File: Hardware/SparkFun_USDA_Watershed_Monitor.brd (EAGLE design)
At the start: 63.5 x 50.8 mm, 113 parts, among them J3 QWIIC_RIGHT_ANGLE, J4 U.FL, Q1 20V/4.2A/52mΩ/1.4W, Q2 20V/0.2A/8MHz/1.2Ω/1Vth, Q3 20V/0.2A/8MHz/1.2Ω/1Vth, Q4 20V/0.2A/8MHz/1.2Ω/1Vth, Q5 20V/0.2A/8MHz/1.2Ω/1Vth, U1 ESP-WROOM-3232D, U10 MMC5983MA_QFN16, U11 RFM9XRFM95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

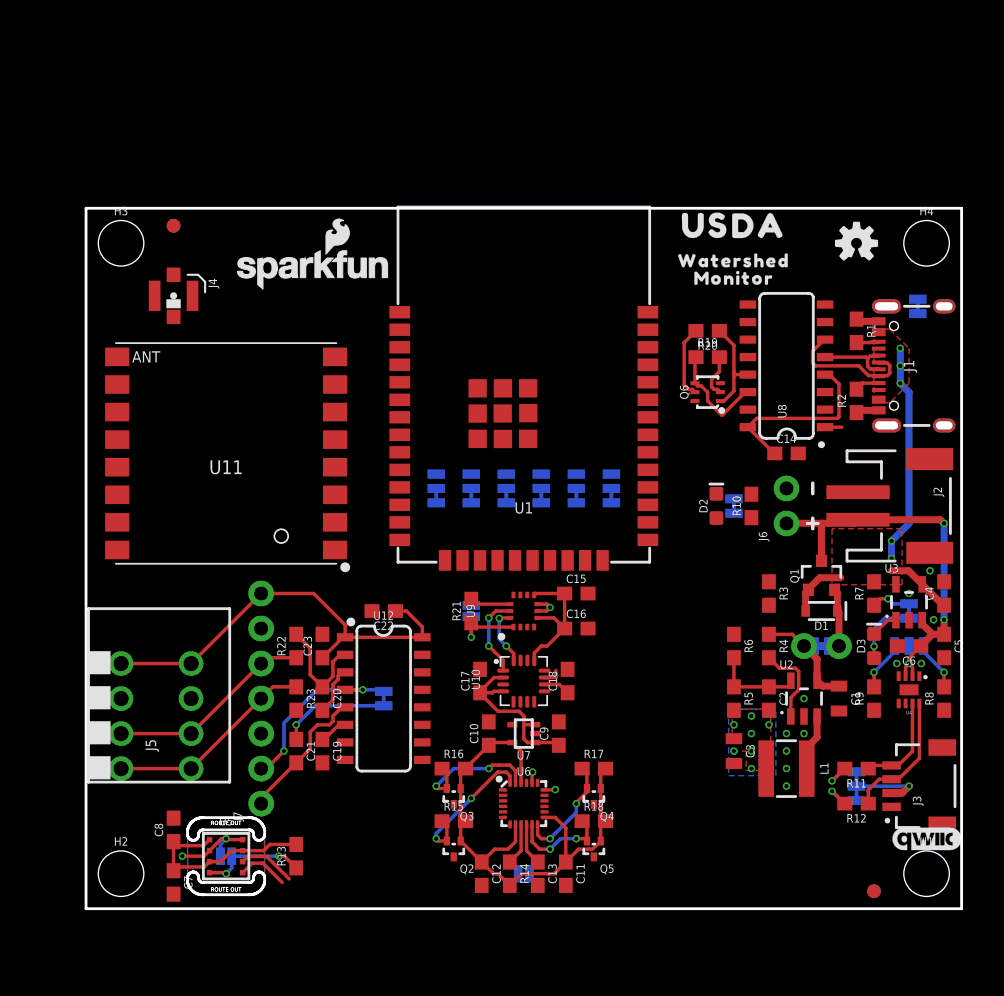
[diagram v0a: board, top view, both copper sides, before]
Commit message: Finish 90% of initial design
Rename Eagle files to match project name
Clean up schematic arrangement
Finish 90% of routing (ESP32 connections will be determined later)
Add Buzzard labels
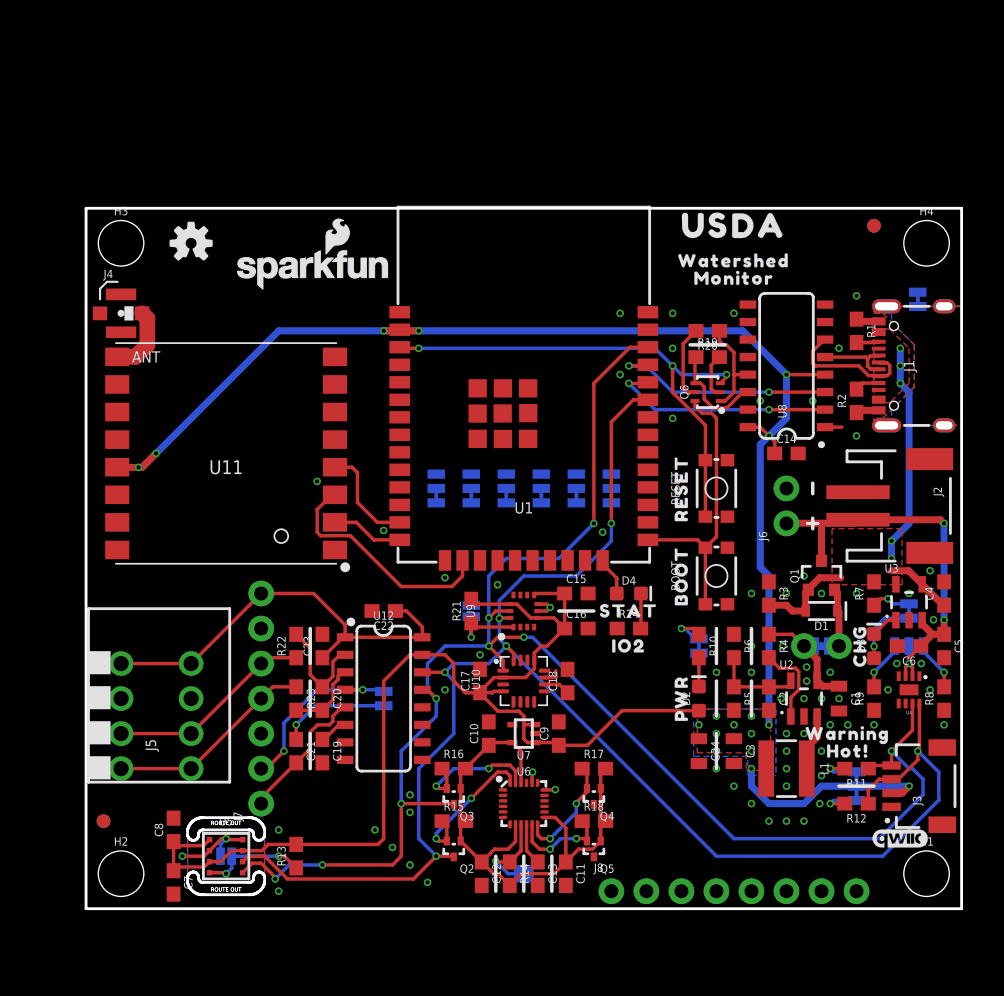
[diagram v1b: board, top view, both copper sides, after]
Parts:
- added BOOT, RESET: MOMENTARY-SWITCH-SPST-SMD-4.6X2.8MM, SparkFun-Switches:TACTILE_SWITCH_SMD_4.6X2.8MM
- added C24: 22uF, SparkFun-Capacitors:0805
- added D4: BLUE, SparkFun-LED:LED-0603
- added J8: (no value), SparkFun-Connectors:1X08_NO_SILK
- added R24: 2.2k, SparkFun-Resistors:0603
- added U$12: (no value), output:#100MA#0
- added U$13: (no value), output:#500MA#0
- added U$14: (no value), output:#CHG#0
- added U$15: (no value), output:#I2C#0
- added U$16: (no value), output:CHG0
- added U$17: (no value), output:#CAP#0
- added U$18: (no value), output:#BME_ADR#0
- added U$19: (no value), output:#ICM_ADR#0
- added U$20: (no value), output:#ISM_ADR#0
- added U$21: (no value), output:#BATTERY#0
- added U$22: (no value), output:#SHLD#0
- added U$23, U$24: (no value), output:WARNING0
- added U$25, U$26: (no value), output:HOT##0
- added U$27: (no value), output:RESET0
- added U$28: (no value), output:BOOT0
- added U$29: (no value), output:PWR0
- added U$30: (no value), output:STAT0
- added U$31: (no value), output:IO20
- added U$9: (no value), output:#MEAS#0
- LOGO3: value QWIIC_LOGO_5MM -> QWIIC_LOGO_4MM; device SparkFun-Aesthetics:QWIIC_5MM -> SparkFun-Aesthetics:QWIIC_4MM
- moved FD1 56.1 mm to (1.27, 6.35)
- moved FD2 56.1 mm to (1.27, 6.35)
- moved FD3 50.8 mm to (57.1, 49.5)
- moved FD4 50.8 mm to (57.1, 49.5)
- moved LOGO2 48.3 mm to (7.62, 48.3)
- moved D2 14.0 mm to (44.5, 15.2)
- moved R10 10.9 mm to (44.5, 19.1), turned to 270 degrees
- moved PWR 10.5 mm to (44.5, 19.1)
- moved J4 4.02 mm to (2.54, 43.2), turned to 0 degrees
- moved LOGO3 1.91 mm to (59.1, 5.08)
- moved SHLD 0.51 mm to (60.3, 44.2)
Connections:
- net N$1 renamed SHLD
- new net N$1: D4.C, R24.2
- net 3.3V: now also C24.1
- net ESP_EN: now also RESET.3, RESET.4
- net ESP_IO0: now also BOOT.3, BOOT.4
- net ESP_IO2: now also D4.A
- net GND: now also BOOT.1, BOOT.2, C24.2, R24.1, RESET.1, RESET.2
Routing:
- net 3.3V: track 59.9 -> 191.6 mm, vias 8 -> 17
- net SCL: track 16.9 -> 122.1 mm, vias 2 -> 9
- net SDA: track 18.1 -> 119.5 mm, vias 2 -> 6
- net ESP_EN: track 0.00 -> 37.3 mm, vias 0 -> 3
- net ESP_IO0: track 0.00 -> 20.5 mm
- net PICO: track 0.00 -> 17.0 mm
- net ESP_TX: track 0.00 -> 16.4 mm, vias 0 -> 2
- net ESP_RX: track 0.00 -> 16.4 mm, vias 0 -> 2
- net SCK: track 0.00 -> 7.61 mm
- net POCI: track 0.00 -> 5.22 mm
- net N$25: track 0.00 -> 4.99 mm
- net N$17: track 3.07 -> 6.09 mm, vias 0 -> 1
- net N$26: track 0.00 -> 3.02 mm, vias 0 -> 1
- net V_USB: track 25.2 -> 28.1 mm
- net ESP_IO2: track 0.00 -> 2.83 mm
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- added copper zone on layer 1, net SHLD
- added copper zone on layer 16, net SHLD

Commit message: Finish initial design
Increase board height from 2 to 2.5 inches
Move LoRa module up, and antenna to top side of board
Replace load cell spring terminal and GPIO header with RJ45 jacks
Add second Qwiic connector to left side of board
Remove fuel gauge
Remove CHG_I jumper, and set charge current to 500mA only
Reroute I2C lines to make room for GPIO going to bottom of the board
Connect and route GPIO lines to bottom RJ45 connectors
Adjust/add buzzard labels
Add region on back silk for board notes
Season with GND vias
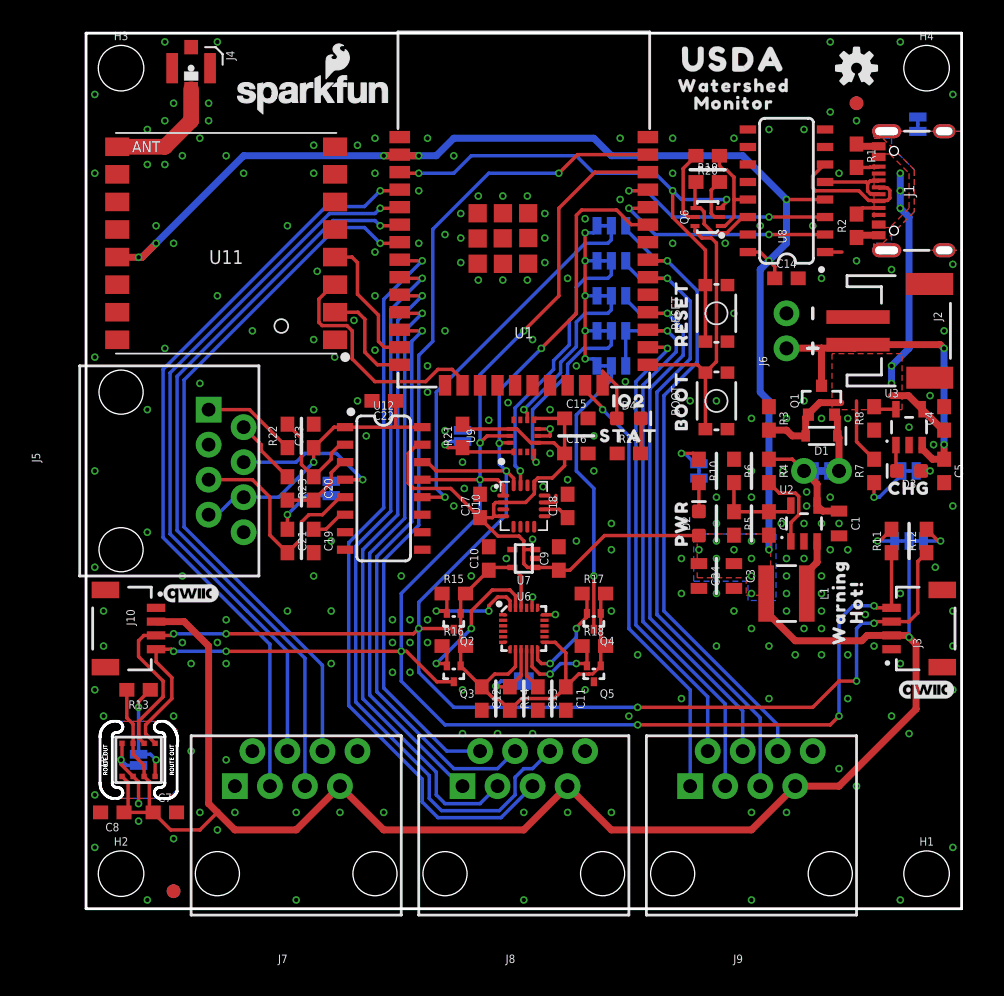
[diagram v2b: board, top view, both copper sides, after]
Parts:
- removed C6: 0.1uF, SparkFun-Capacitors:0603
- removed CHG_I, MAX_INT: JUMPER-SMT_3_1-NC_TRACE_SILK, SparkFun-Jumpers:SMT-JUMPER_3_1-NC_TRACE_SILK
- removed R9: 10k, SparkFun-Resistors:0603
- removed U4: MAX17048, SparkFun-IC-Power:DFN-8
- added J10: QWIIC_RIGHT_ANGLE, SparkFun-Connectors:JST04_1MM_RA
- added J9: RJ45, SparkFun-Connectors:RJ45-8
- added LOGO4: QWIIC_LOGO_4MM, SparkFun-Aesthetics:QWIIC_4MM
- added U$32: (no value), output:ORW0
- added U$33: (no value), output:OR0
- added U$34: (no value), output:GRW0
- added U$35: (no value), output:GR0
- added U$36: (no value), output:BLW0
- added U$37: (no value), output:BL0
- added U$38: (no value), output:BRW0
- added U$39: (no value), output:BR0
- added U$40: (no value), output:A#1
- added U$41: (no value), output:B#0
- added U$42: (no value), output:B#1
- added U$43: (no value), output:E#0
- added U$44: (no value), output:E#1
- added U$45: (no value), output:#RJ45_COLORS#0
- added U$46: (no value), output:#PWR#0
- added U$47, U$48: (no value), output:NC0
- added U$49: (no value), output:IO270
- added U$50: (no value), output:IO260
- added U$51: (no value), output:IO230
- added U$52: (no value), output:IO250
- added U$53: (no value), output:IO320
- added U$54: (no value), output:IO330
- added U$55: (no value), output:IO150
- added U$56: (no value), output:IO40
- added U$57: (no value), output:IO160
- added U$58: (no value), output:IO170
- added U$59: (no value), output:IO180
- added U$60: (no value), output:IO190
- added U$61: (no value), output:I340
- added U$62: (no value), output:I350
- added U$63: (no value), output:I360
- added U$64: (no value), output:I390
- added U$65: (no value), output:#IO19#0
- added U$66: (no value), output:#IO18#0
- added U$67: (no value), output:#IO17#0
- added U$68, U$69: (no value), output:#IO16#0
- added U$70: (no value), output:#NAU_INT#0
- added U$71: (no value), output:#MMC_INT#0
- added U$72: (no value), output:#ISM_INT2#0
- added U$73: (no value), output:#ISM_INT1#0
- added U$74: (no value), output:#ICM_INT#0
- added U$75: (no value), output:#IO#0
- added U$76: (no value), output:##INT##0
- added U$77: (no value), output:#NOTES#0
- J5: value (none) -> RJ45; device SparkFun-Connectors:1X04_SPRING_TERMINAL -> SparkFun-Connectors:RJ45-8
- J7: value (none) -> RJ45; device SparkFun-Connectors:1X07_NO_SILK -> SparkFun-Connectors:RJ45-8
- J8: value (none) -> RJ45; device SparkFun-Connectors:1X08_NO_SILK -> SparkFun-Connectors:RJ45-8
- U$10: device output:#B#_#0 -> output:3V30
- U$11: device output:#B#_#1 -> output:GND0
- U$12: device output:#100MA#0 -> output:A#0
- U$13: device output:#500MA#0 -> output:VDD0
- U$4: device output:#RED#E#_#0 -> output:GND0
- U$5: device output:#BLK#E#_#0 -> output:3V30
- U$6: device output:#WHT#A#_#0 -> output:GND0
- U$7: device output:#GRN#A#_#0 -> output:3V30
- U$8: device output:#YLW#SD_#0 -> output:GND0
- moved U$13 58.4 mm to (1.52, 29.8)
- moved U$12 55.7 mm to (6.10, 29.8)
- moved LOGO2 49.9 mm to (55.9, 61.0)
- moved U$10 38.0 mm to (50.2, 1.52)
- moved U$8 35.5 mm to (46.4, 1.52)
- moved U$11 26.0 mm to (1.52, 33.7), turned to 90 degrees
- moved U$7 25.0 mm to (33.7, 1.52)
- moved U$6 23.6 mm to (29.8, 1.52)
- moved J5 21.7 mm to (2.54, 31.8), turned to 270 degrees
- moved U$4 21.3 mm to (13.3, 1.52)
- moved R8 20.9 mm to (57.1, 35.6)
- moved R12 19.7 mm to (61.0, 26.7), turned to 90 degrees
- moved U$15 19.6 mm to (59.7, 28.3), turned to 0 degrees
- moved U$5 19.3 mm to (17.1, 1.52)
- moved NAU_INT 19.1 mm to (38.1, 49.5), turned to 0 degrees
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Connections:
- removed net !MAX_INT!: MAX_INT.2, U4.5
- removed net N$12: CHG_I.1, R8.2
- net !INT!: no longer MAX_INT.3
- net 3.3V: now also J10.2, J7.7, J8.7, J9.7
- net ESP_I34: now also J7.5
- net ESP_I35: now also J7.6
- net ESP_I36: now also J7.3
- net ESP_I39: now also J7.4
- net ESP_IO15: now also J9.1
- net ESP_IO16: now also ICM_INT.1, ISM_INT1.1, J9.3; no longer MAX_INT.1
- net ESP_IO17: now also ISM_INT2.1, J9.4; no longer ICM_INT.1, ISM_INT1.1
- net ESP_IO18: now also J9.5, MMC_INT.1; no longer ISM_INT2.1
- net ESP_IO19: now also J9.6, NAU_INT.1; no longer MMC_INT.1
- net ESP_IO23: now also J8.2; no longer NAU_INT.1
- net ESP_IO25: now also J8.3
- net ESP_IO26: now also J8.1
- net ESP_IO27: now also J8.4
- net ESP_IO32: now also J8.5
- net ESP_IO33: now also J8.6
- net ESP_IO4: now also J9.2
- net GND: now also J10.1, J5.3, J5.8, J7.8, J8.8, J9.8; no longer C6.2, J5.2, J5.6, J7.3, J7.6, R9.1, U4.1, U4.4, U4.6, U4.9
- net N$11: now also R8.2, U3.5; no longer CHG_I.3, R9.2
- net NAU_A+: now also J5.2; no longer J5.4, J5.8, J7.4
- net NAU_A-: now also J5.1; no longer J5.3, J5.7, J7.5
- net NAU_B+: now also J5.5; no longer J7.1
- net NAU_B-: now also J5.4; no longer J7.2
- net SCL: now also J10.4; no longer U4.7
- net SDA: now also J10.3; no longer U4.8
- net VDDA: now also J5.6, J5.7; no longer J5.1, J5.5, J7.7
- net V_BATT: no longer C6.1, CHG_I.2, U4.2, U4.3
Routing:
- net 3.3V: track 191.6 -> 266.7 mm
- net ESP_IO23: track 0.00 -> 61.5 mm, vias 0 -> 1
- net ESP_I36: track 0.00 -> 56.0 mm, vias 0 -> 1
- net ESP_IO33: track 0.00 -> 55.3 mm, vias 0 -> 1
- net ESP_IO32: track 0.00 -> 54.8 mm, vias 0 -> 1
- net ESP_I34: track 0.00 -> 54.6 mm, vias 0 -> 1
- net ESP_I39: track 0.00 -> 52.6 mm, vias 0 -> 1
- net ESP_I35: track 0.00 -> 51.8 mm, vias 0 -> 1
- net ESP_IO25: track 0.00 -> 47.1 mm, vias 0 -> 1
- net ESP_IO18: track 0.00 -> 46.8 mm, vias 0 -> 1
- net ESP_IO19: track 0.00 -> 46.5 mm, vias 0 -> 1
- net ESP_IO16: track 0.00 -> 43.8 mm, vias 0 -> 1
- net ESP_IO27: track 0.00 -> 42.1 mm, vias 0 -> 1
- net ESP_IO17: track 0.00 -> 41.2 mm, vias 0 -> 1
- net ESP_IO26: track 0.00 -> 40.4 mm, vias 0 -> 1
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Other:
- board size 63.5 x 50.8 mm -> 63.5 x 63.5 mm

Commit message: Cleanup design
Connect interrupt net to IO4
Connect V_BATT to IO32 pin through voltage divider to measure battery voltage
Increase 3V3 trace width to 25 mils on low half of board
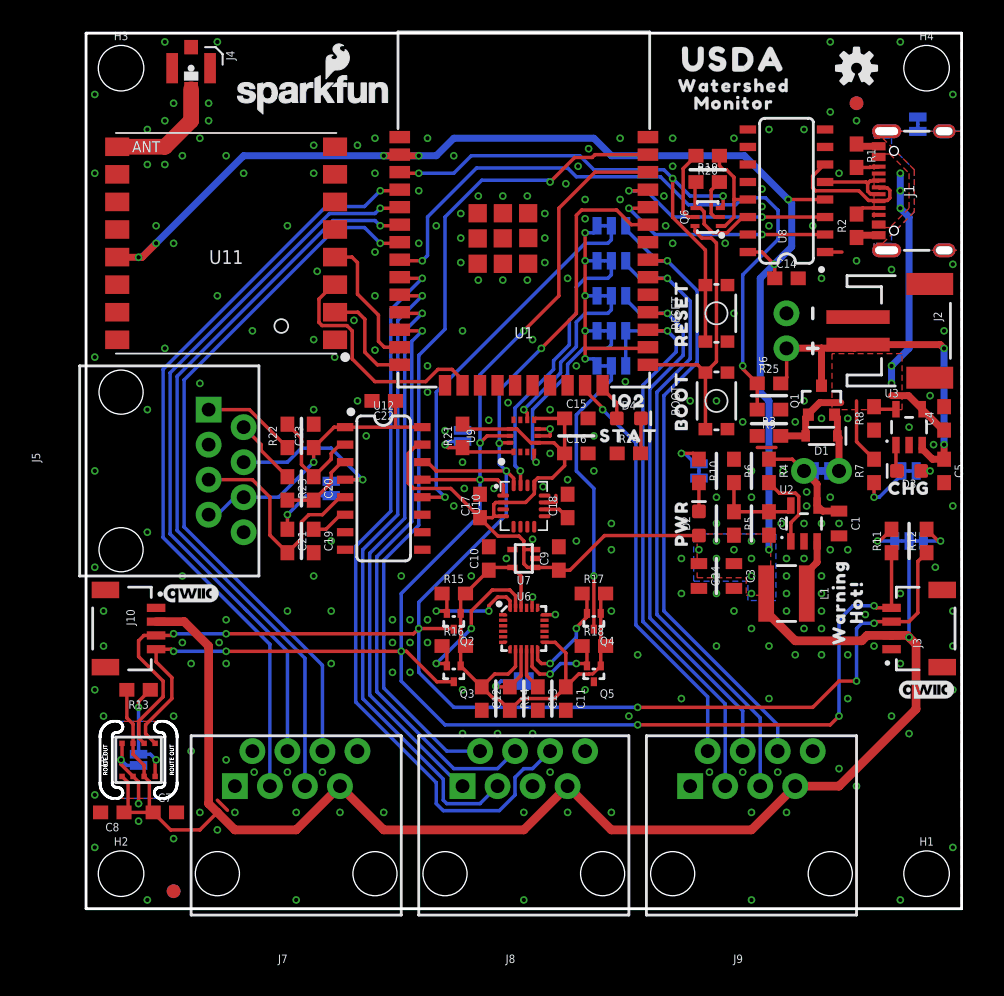
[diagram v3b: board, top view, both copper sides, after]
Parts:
- removed U$53: (no value), output:IO320
- added R25, R9: 100k, SparkFun-Resistors:0603
- added U$78: (no value), output:IO230
- U$51: device output:IO230 -> output:NC0
- U$56: device output:IO40 -> output:NC0
- moved U$51 4.88 mm to (33.7, 3.05)
- moved U$55 3.81 mm to (46.4, 6.10)
- moved U$56 3.81 mm to (50.2, 6.10)
- moved R3 1.27 mm to (49.5, 34.3), turned to 0 degrees
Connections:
- removed net !INT!: ICM_INT.3, ISM_INT1.3, ISM_INT2.3, MMC_INT.3, NAU_INT.3
- net ESP_IO15: now also J9.2; no longer J9.1
- net ESP_IO32: now also R25.1, R9.2; no longer J8.5
- net ESP_IO4: now also ICM_INT.3, ISM_INT1.3, ISM_INT2.3, MMC_INT.3, NAU_INT.3; no longer J9.2
- net GND: now also R9.1
- net V_BATT: now also R25.2
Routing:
- net ESP_IO4: track 33.8 -> 18.8 mm, vias 1 -> 5
- net !INT!: track 14.2 -> 0.00 mm, vias 5 -> 0
- net ESP_IO32: track 54.8 -> 49.5 mm, vias 1 -> 2
- net V_BATT: track 24.6 -> 27.3 mm
- net GND: track 16.2 -> 18.6 mm, vias 230 -> 245
- net ESP_IO2: track 4.86 -> 2.83 mm
- net ESP_IO15: track 32.2 -> 30.2 mm
- net V_USB: track 32.8 -> 31.8 mm
- net ESP_EN: track 38.3 -> 39.0 mm
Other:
- outline, holes or cut-outs redrawn
